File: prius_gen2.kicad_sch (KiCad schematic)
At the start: 42 parts, among them J2 Conn_01x06, SW1 SW_Push, SW2 SW_Push, U1 STM32F407VETx, Y1 8MHz

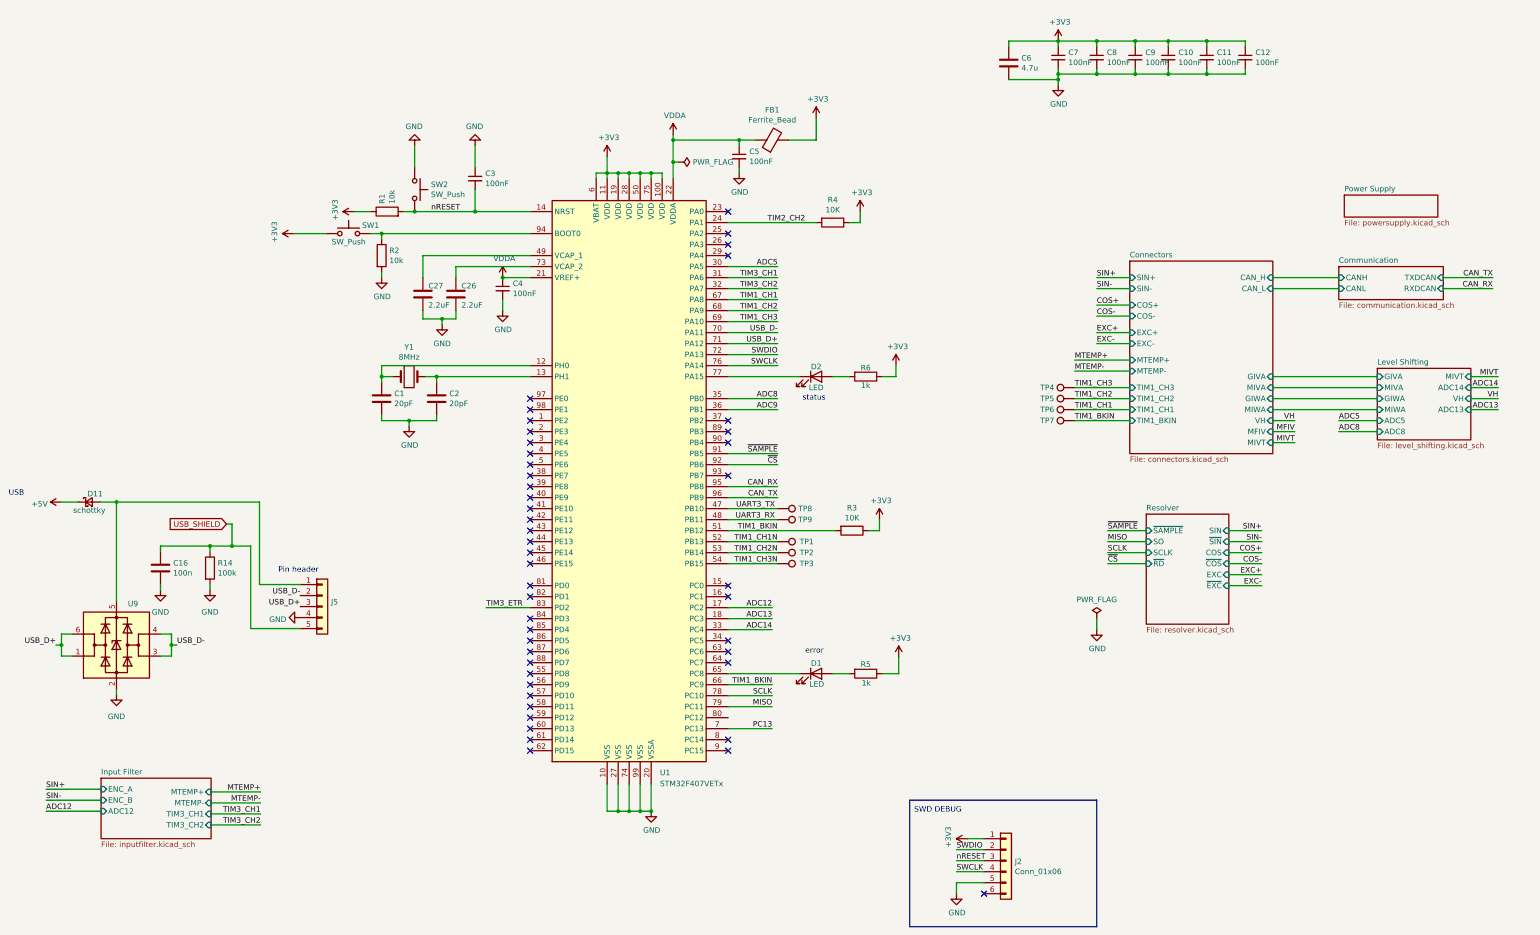
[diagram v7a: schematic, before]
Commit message: fixed adcs
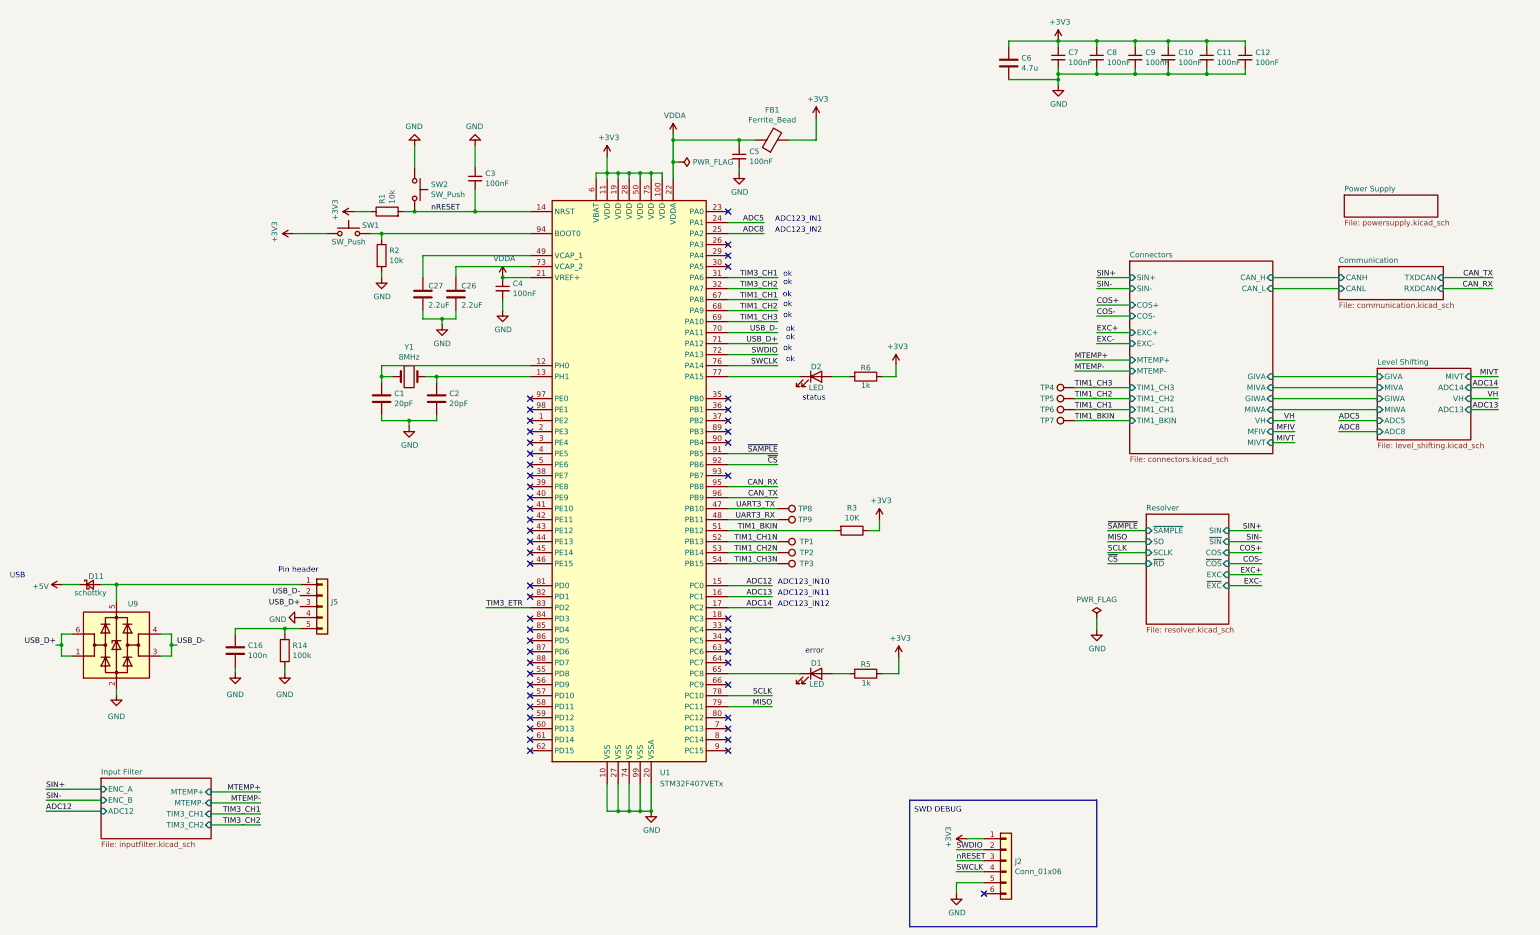
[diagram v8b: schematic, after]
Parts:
- removed R4: 10K, Resistor_SMD:R_0603_1608Metric, symbol Device:R
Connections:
- net TIM2_CH2 is gone; now on net ADC5: U1.24 (PA1)
- net ADC12: now also U1.15 (PC0); no longer U1.17 (PC2)
- net ADC13: now also U1.16 (PC1); no longer U1.18 (PC3)
- net ADC14: now also U1.17 (PC2); no longer U1.33 (PC4)
- net ADC5: no longer U1.30 (PA5)
- net ADC8: now also U1.25 (PA2); no longer U1.35 (PB0)
- net TIM1_BKIN: no longer U1.66 (PC9)
- net ADC9: no longer names the net of U1.36 (PB1)
- net PC13: no longer names the net of U1.7 (PC13)
- net USB_SHIELD: no longer names the net of C16.1, J5.5 (Pin_5), R14.1
- no-connect marks 47 -> 52
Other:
- note added: "ADC123_IN1"
- note added: "ADC123_IN10"
- note added: "ADC123_IN11"
- note added: "ADC123_IN12"
- note added: "ADC123_IN2"
- note added: "ok"
- moved on the sheet: C16, D11, R14
